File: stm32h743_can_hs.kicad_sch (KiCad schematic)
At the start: 100 parts, among them J1 Conn_02x38_Counter_Clockwise, J2 Conn_02x38_Counter_Clockwise, J3 USB_C_Receptacle_USB2.0_16P, J4 USB_C_Receptacle_USB2.0_16P, J5 DE9_Pins_MH, J6 Conn_01x05_Pin, J7 Conn_ARM_JTAG_SWD_10, Q1 BSS138, Q2 BSS138, Q3 BSS138, SW1 SW_Push, SW2 SW_Push, U1 STM32H743IITx, U2 ST1S40IDR, U3 TPS2121RUX, U4 USB3300-EZK, U5 MCP2562-E-SN, U6 W25Q128JVS, Y1 SG-210STF, Y2 8MHz, Y3 Crystal

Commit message: add hugo docs
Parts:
- D3: Part Number (none) -> 150141M173100
- R21, R22: Part Number (none) -> RC0402FR-075R1L
- R23: Part Number (none) -> RC0402FR-0768RL
- R27: Part Number (none) -> RC0402FR-07300RL

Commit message: via stitching, fix PF7, docs license
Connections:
- net GND: no longer J1.60 (Pin_60)
- net PF7: now reaches U1.25 (PF7)
- net PF7: now also J1.60 (Pin_60)

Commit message: bom changes
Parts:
- C1, C10, C11, C12, C13, C14, C19, C2, C20, C22, C23, C24, C26, C27, C28, C29, C3, C30, C31, C34, C35, C4, C41, C5, C6, C7, C8, C9: Part Number GRM155R71H104KE14D -> (none); manf# (none) -> GRM155R71H104KE14D
- C15: Part Number GRM188R61A106ME69D -> (none); manf# (none) -> GRM188R61A106ME69D
- C16: Part Number GRM188R61A105KA61D -> (none); manf# (none) -> GRM188R61A105KA61D
- C17: Part Number GRM1555C1H180FA01D -> (none); manf# (none) -> GRM1555C1H180FA01D
- C18: Part Number GRM188R60J226MEA0J -> (none); manf# (none) -> GRM188R60J226MEA0J
- C21: Part Number GRM155R71C103KA01D -> (none); manf# (none) -> GRM155R71C103KA01D
- C25: Part Number GRM155R60J475ME47D -> (none); manf# (none) -> GRM155R60J475ME47D
- C32, C33: Part Number GRM155C80J225KE95D -> (none); manf# (none) -> GRM155C80J225KE95D
- C36, C37: Part Number GCM1555C1H220JA16D -> (none); manf# (none) -> GCM1555C1H220JA16D
- C38: Part Number GRM155R71H472KA01D -> (none); manf# (none) -> GRM155R71H472KA01D
- C39, C40: Part Number GRM1555C1H470JA01D -> (none); manf# (none) -> GRM1555C1H470JA01D
- D1, D2: Part Number MMBZ27VCLT1G -> (none); manf# (none) -> MMBZ27VCLT1G
- D3: Part Number 150141M173100 -> (none); manf# (none) -> 150141M173100
- D4: Part Number LTST-C190KRKT -> (none); manf# (none) -> LTST-C190KRKT
- FB1: Part Number BBHV00160808601Y00 -> (none); manf# (none) -> BBHV00160808601Y00
- J1, J2: Part Number PREC040DAAN-RC, Cut down to 2x38 -> (none); manf# (none) -> PREC040DAAN-RC
- J3, J4: Part Number USB4105-GF-A -> (none); manf# (none) -> USB4105-GF-A
- J5: Part Number A-DS 09 A/KG-T2S -> (none); manf# (none) -> A-DS 09 A/KG-T2S
- J6: Part Number 10129378-905001BLF -> (none); manf# (none) -> 10129378-905001BLF
- J7: Part Number FTSH-105-01-L-DV-K -> (none); manf# (none) -> FTSH-105-01-L-DV-K
- L1: Part Number VLS6045EX-3R3N -> (none); manf# (none) -> VLS6045EX-3R3N
- Q1, Q2, Q3: Part Number BSS138PW,115 -> (none); manf# (none) -> BSS138PW,115
- R1: value 75k -> 75k 1%; Part Number RC0402FR-0775KL -> (none); manf# (none) -> RC0402FR-0775KL
- R10, R11, R2: value 24k -> 24k 1%; Part Number RC0402FR-0724KL -> (none); manf# (none) -> RC0402FR-0724KL
- R12, R17, R18: Part Number RC0402JR-070RL -> (none); manf# (none) -> RC0402JR-070RL
- R13, R24, R25, R26: Part Number RC0402JR-071KL -> (none); manf# (none) -> RC0402JR-071KL
- R14: Part Number RC0402FR-0712KL -> (none); manf# (none) -> RC0402FR-0712KL
- R15, R16: Part Number RC0402JR-0710KL -> (none); manf# (none) -> RC0402JR-0710KL
- R19, R20: value 60.4R -> 60.4R 1%; Part Number RC0402FR-0760R4L -> (none); manf# (none) -> RC0402FR-0760R4L
- R21, R22: Part Number RC0402FR-075R1L -> (none); manf# (none) -> RC0402JR-075R1L
- R23: Part Number RC0402FR-0768RL -> (none); manf# (none) -> RC0402JR-0768RL
- R27: Part Number RC0402FR-07300RL -> (none); manf# (none) -> RC0402JR-07300RL
- R3: Part Number RC0402FR-0730KL -> (none); manf# (none) -> RC0402JR-0730KL
- R4, R5, R6, R7, R8, R9: Part Number RC0402FR-075K1L -> (none); manf# (none) -> RC0402JR-075K1L
- SW1, SW2: Part Number PTS815SJM250SMTRLFS -> (none); manf# (none) -> PTS815SJM250SMTRLFS
- U1: Part Number STM32H743IIT6 -> (none); manf# (none) -> STM32H743IIT6
- U2: Part Number ST1S40IDR -> (none); manf# (none) -> ST1S40IDR
- U3: Part Number TPS2121RUXR -> (none); manf# (none) -> TPS2121RUXR
- U4: Part Number USB3300-EZK -> (none); manf# (none) -> USB3300-EZK
- U5: Part Number MCP2562-E/SN -> (none); manf# (none) -> MCP2562-E/SN
- U6: value W25Q128JVS -> S25FL128LAGMFI013; Part Number W25Q128JVSIQ TR -> (none); manf# (none) -> S25FL128LAGMFI013
- Y1: Part Number SG-210STF 24.0000ML0 -> (none); manf# (none) -> SG-210STF 24.0000ML0
- Y2: Part Number SG-210STF 8.0000ML0 -> (none); manf# (none) -> SG-210STF 8.0000ML0
- Y3: Part Number FC-135 32.7680KA-A5 -> (none); manf# (none) -> FC-135 32.7680KA-A5
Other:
- moved on the sheet: C41

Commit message: cleanup, board rev
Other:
- company: (none) -> Kevinbot
- title: (none) -> STM32H743 CAN + USB-HS Dev Board
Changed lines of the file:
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@@
 	(generator_version "10.0")
 	(paper "A2")
+	(title_block
+		(title "STM32H743 CAN + USB-HS Dev Board")
+		(date "2026-07-17")
+		(rev "1.0")
+		(company "Kevinbot")
+		(comment 1 "Licensed under the GNU GPL-3.0")
+	)
 	(text_box "VBUS Switch"
 		(exclude_from_sim no)

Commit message: fix field warnings, erc, drc, vias
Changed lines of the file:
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@@
 	(wire
 		(pts
-			(xy 299.72 177.8) (xy 287.02 177.8)
-		)
-		(stroke
-			(width 0)
-			(type default)
-		)
-	)
-	(wire
-		(pts
 			(xy 237.49 148.59) (xy 242.57 153.67)
 		)
@@
 	(wire
 		(pts
-			(xy 299.72 180.34) (xy 287.02 180.34)
-		)
-		(stroke
-			(width 0)
-			(type default)
-		)
-	)
-	(wire
-		(pts
 			(xy 171.45 60.96) (xy 171.45 63.5)
 		)
@@
 		)
 	)
-	(label "CAN_TX"
-		(at 299.72 180.34 180)
-		(effects
-			(font
-				(size 1.27 1.27)
-			)
-			(justify right bottom)
-		)
-	)
 	(label "PI0"
 		(at 72.39 156.21 90)
@@
 		)
 	)
-	(label "PI9"
+	(label "CAN_RX"
 		(at 95.25 156.21 90)
 		(effects
@@
 		)
 	)
-	(label "PH13"
+	(label "CAN_TX"
 		(at 138.43 160.02 90)
 		(effects
@@
 		)
 	)
-	(label "CAN_RX"
-		(at 299.72 177.8 180)
-		(effects
-			(font
-				(size 1.27 1.27)
-			)
-			(justify right bottom)
-		)
-	)
 	(label "PD7"
 		(at 346.71 45.72 0)
@@
 		(effects
 			(font
-				(size 1.27 1.27)
-			)
-			(justify left bottom)
-		)
-	)
-	(label "PH13"
-		(at 287.02 180.34 0)
-		(effects
-			(font
-				(size 1.27 1.27)
-			)
-			(justify left bottom)
-		)
-	)
-	(label "PI9"
-		(at 287.02 177.8 0)
-		(effects
-			(font

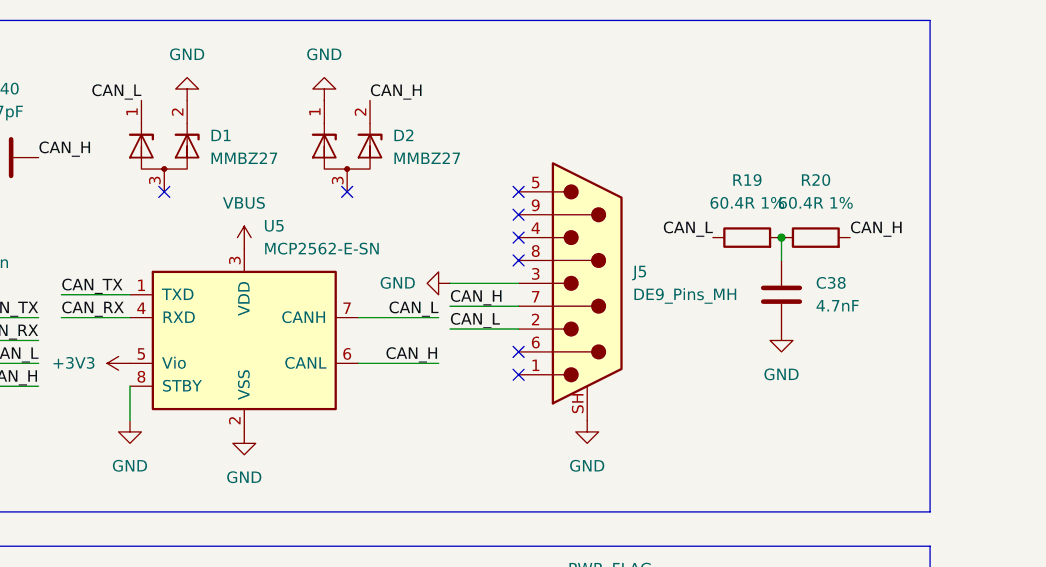
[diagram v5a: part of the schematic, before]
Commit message: board cleanup, change can xciever to TI
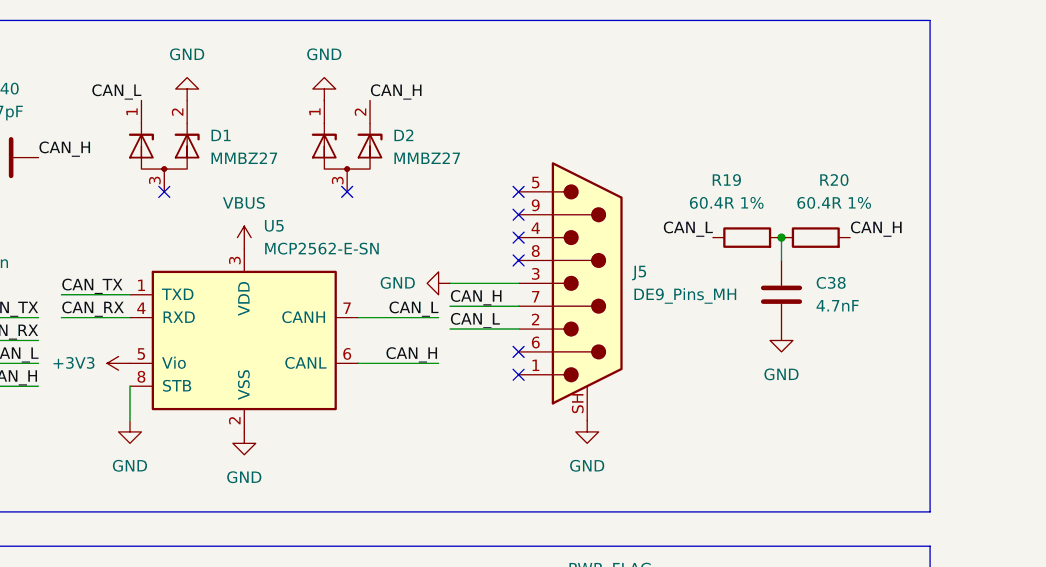
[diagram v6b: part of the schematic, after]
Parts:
- U5: symbol Interface_CAN_LIN:MCP2562-E-SN -> Interface_CAN_TI:TCAN1044AEV; manf# MCP2562-E/SN -> TCAN1044AVDRQ1
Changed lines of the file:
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@@
 	)
 	(symbol
-		(lib_id "Interface_CAN_LIN:MCP2562-E-SN")
+		(lib_id "Interface_CAN_TI:TCAN1044AEV")
 		(at 330.2 167.64 0)
 		(unit 1)
@@
 			)
 		)
-		(property "Datasheet" "http://ww1.microchip.com/downloads/en/DeviceDoc/25167A.pdf"
+		(property "Datasheet" "https://www.ti.com/lit/ds/symlink/tcan1044aev-q1.pdf"
 			(at 330.2 167.64 0)
 			(hide yes)
@@
 			)
 		)
-		(property "Description" "High-Speed CAN Transceiver, 1Mbps, 5V supply, Vio pin, -40C to +125C, SOIC-8"
+		(property "Description" "High-Speed CAN Transceiver, 1Mbps, 5V supply, Vio pin, -40C to +150C, SOIC-8"
 			(at 330.2 167.64 0)
 			(hide yes)
@@
 			)
 		)
-		(property "manf#" "MCP2562-E/SN"
+		(property "manf#" "TCAN1044AVDRQ1"
 			(at 330.2 167.64 0)
 			(hide yes)
@@
 		(in_pos_files yes)
 		(dnp no)
-		(fields_autoplaced yes)
 		(property "Reference" "R20"
-			(at 393.7 149.86 90)
+			(at 395.732 149.86 90)
 			(show_name no)
 			(do_not_autoplace no)
@@
 		)
 		(property "Value" "60.4R 1%"
-			(at 393.7 152.4 90)
+			(at 395.732 152.4 90)
 			(show_name no)
 			(do_not_autoplace no)
@@
 		(in_pos_files yes)
 		(dnp no)
-		(fields_autoplaced yes)
 		(property "Reference" "R19"
-			(at 386.08 149.86 90)
+			(at 383.794 149.86 90)
 			(show_name no)
 			(do_not_autoplace no)
@@
 		)
 		(property "Value" "60.4R 1%"
-			(at 386.08 152.4 90)
+			(at 383.794 152.4 90)
 			(show_name no)
 			(do_not_autoplace no)

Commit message: cleanup
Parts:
- U5: value MCP2562-E-SN -> TCAN1044AVDRQ1
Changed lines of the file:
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@@
 			)
 		)
-		(property "Value" "MCP2562-E-SN"
+		(property "Value" "TCAN1044AVDRQ1"
 			(at 332.3433 157.48 0)
 			(show_name no)

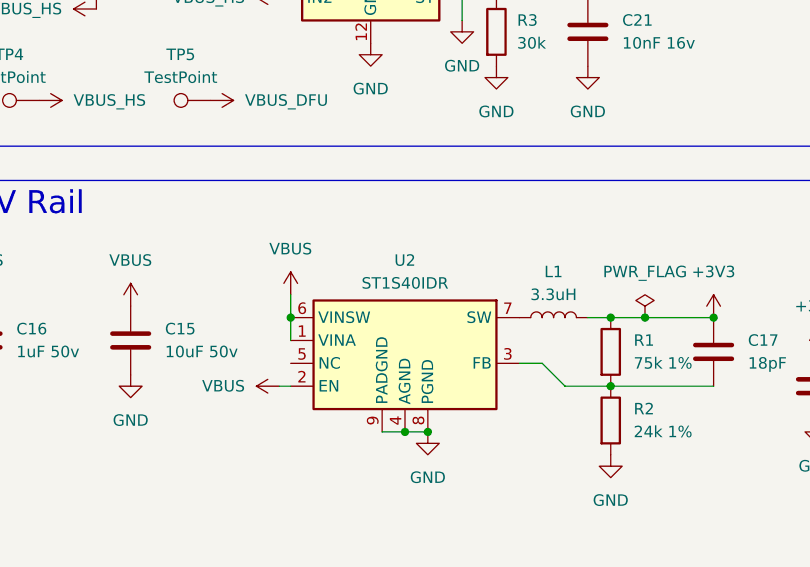
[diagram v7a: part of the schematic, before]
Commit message: fix buck ic part numbers
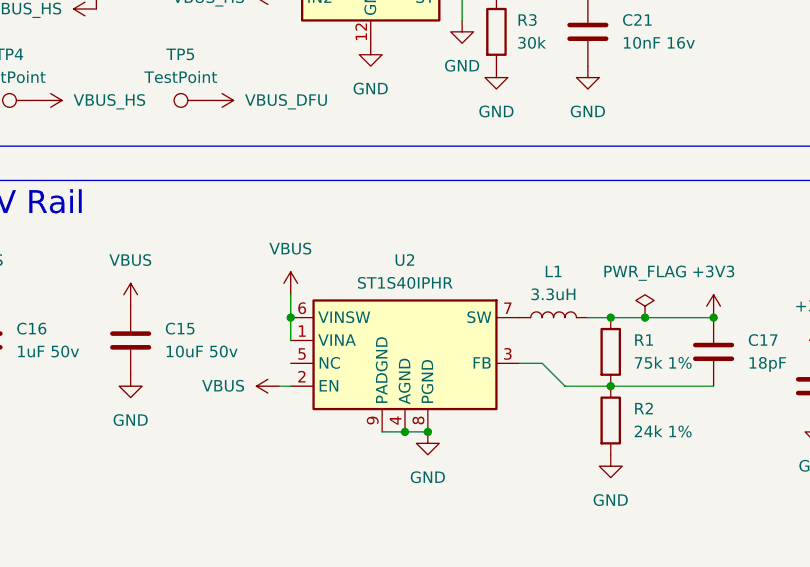
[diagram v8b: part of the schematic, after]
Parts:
- U2: value ST1S40IDR -> ST1S40IPHR; symbol Regulator_Switching_ST:ST1S40IDR -> Regulator_Switching_ST:ST1S40IPHR; manf# ST1S40IDR -> ST1S40IPHR
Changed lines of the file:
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@@
 	)
 	(symbol
-		(lib_id "Regulator_Switching_ST:ST1S40IDR")
+		(lib_id "Regulator_Switching_ST:ST1S40IPHR")
 		(at 68.58 255.27 0)
 		(unit 1)
@@
 			)
 		)
-		(property "Value" "ST1S40IDR"
+		(property "Value" "ST1S40IPHR"
 			(at 68.58 248.92 0)
 			(show_name no)
@@
 			)
 		)
-		(property "manf#" "ST1S40IDR"
+		(property "manf#" "ST1S40IPHR"
 			(at 68.58 255.27 0)
 			(hide yes)
